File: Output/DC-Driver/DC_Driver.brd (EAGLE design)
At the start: 20 x 13 mm, 6 parts, among them IC3 BD6231F

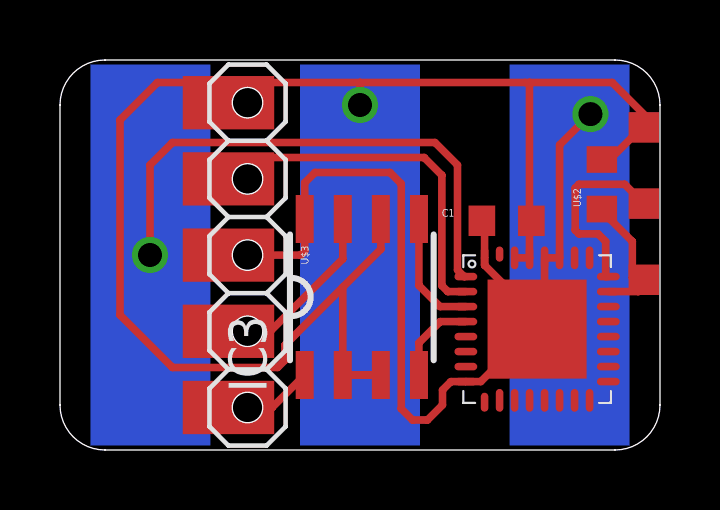
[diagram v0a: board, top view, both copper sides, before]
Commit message: Update Pinheader
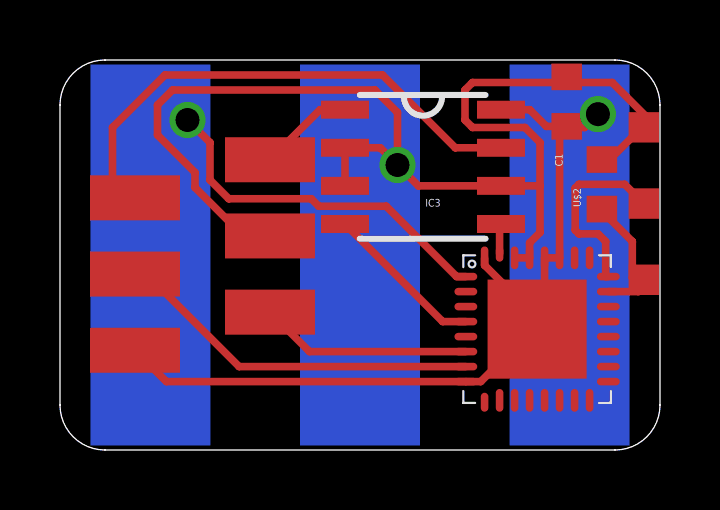
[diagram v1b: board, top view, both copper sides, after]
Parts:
- removed U$3: PINHD_52.54MOD, thar:PINHD_5_MOD
- added U$4: PINHD_6MICROMATCH, thar:MICROMATCH6POL
- moved IC3 4.79 mm to (13.8, 10.7), turned to 270 degrees
- moved C1 4.45 mm to (18.6, 12.9), turned to 270 degrees
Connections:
- new net N$13: U$10.6, U$4.P$2
- new net N$14: U$10.7, U$4.P$3
- net GND: now also U$4.P$1; no longer U$3.P$3
- net N$11: no longer U$3.P$2
- net N$2: now also U$4.P$5; no longer U$3.P$4
- net N$5: now also U$4.P$6; no longer U$3.P$5
- net N$7: now also U$10.31; no longer U$10.3
- net VCC: now also U$4.P$4; no longer U$3.P$1
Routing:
- net N$11: track 12.9 -> 0.00 mm
- net N$14: track 0.00 -> 12.3 mm
- net N$2: track 6.14 -> 17.8 mm
- net VCC: track 61.2 -> 52.6 mm
- net GND: track 50.5 -> 42.6 mm
- net N$13: track 0.00 -> 7.07 mm
- net N$7: track 4.07 -> 1.02 mm
- net N$12: track 19.0 -> 22.0 mm
- net N$6: track 2.93 -> 5.38 mm
